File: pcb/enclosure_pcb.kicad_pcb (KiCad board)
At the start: 2 copper layers, 77.2 x 72.2 mm, 95 parts, among them J1 Conn_01x03_Pin, J3 USB_C_Receptacle_USB2.0_14P, J4 Conn_01x03_Pin, J5 Conn_01x03_Pin, J6 Conn_02x12_Odd_Even, J7 Conn_01x04_Pin, J8 Conn_ARM_JTAG_SWD_10, Q1 S8050, Q2 2SC3357-T1-A, Q3 MMBT918, SW1 SW_Push_WE, SW2 SW_Lever_RSPRO_5MS1, SW3 SW_Push_WE, U1 STM32F446RETx, U2 LD1117S33TR_SOT223, U3 LD1117S50TR_SOT223, U4 USBLC6-4SC6, U6 LM358_C5252902, Y1 Crystal_GND3, Y2 Crystal_4-pin

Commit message: V2_avant_revision
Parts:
- moved R23 158.8 mm to (161.5, 45.7), turned to -90 degrees
- moved J7 134.4 mm to (173.1, 66.0), turned to -90 degrees
- moved Y1 123.8 mm to (111.1, 52.5), turned to 90 degrees
- moved J5 116.2 mm to (125.1, 62.6), turned to 90 degrees
- moved R21 93.2 mm to (143.1, 75.5), turned to 90 degrees
- moved C27 89.3 mm to (197.9, 113.9), turned to 90 degrees
- moved F2 87.9 mm to (193.5, 103.4), turned to 180 degrees
- moved R29 81.6 mm to (146.7, 127.7), turned to 90 degrees
- moved D9 80.3 mm to (184.2, 108.1)
- moved C14 79.6 mm to (185.2, 102.4), turned to 180 degrees
- moved J1 78.6 mm to (145.6, 98.0), turned to -90 degrees
- moved U4 77.5 mm to (157.1, 123.5)
- moved R26 76.1 mm to (143.8, 127.7), turned to 90 degrees
- moved R28 75.0 mm to (140.5, 127.7), turned to 90 degrees
- moved U2 73.6 mm to (191.3, 111.0), turned to 90 degrees
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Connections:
- J6 pad 15: /SCH_MCU/PA2 -> /SCH_MCU/PA0
- J6 pad 19: /SCH_MCU/PA0 -> /SCH_MCU/PA2
- J6 pad 5: /SCH_MCU/PC6 -> /SCH_MCU/PC8
- J6 pad 9: /SCH_MCU/PC8 -> /SCH_MCU/PC6
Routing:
- net +5V: track 180.8 -> 352.2 mm, vias 7 -> 6
- net +3V3: track 254.6 -> 327.7 mm, vias 13 -> 4
- net /SCH_MCU/USB_DN: track 35.3 -> 93.6 mm, vias 0 -> 4
- net /SCH_MCU/USB_DP: track 35.3 -> 90.6 mm, vias 0 -> 2
- net /SCH_MCU/SWO: track 0.00 -> 44.5 mm, vias 0 -> 2
- net (no net): track 41.8 -> 0.00 mm, vias 2 -> 0
- net /SCH_FS1000/DATA IN: track 18.8 -> 60.3 mm
- net /SCH_MCU/PWM: track 26.9 -> 67.9 mm, vias 2 -> 0
- net /SCH_MCU/SWDIO: track 23.5 -> 56.8 mm
- net /SCH_FS1000/DATA OUT: track 27.7 -> 55.8 mm
- net Net-(D9-K): track 0.00 -> 27.4 mm
- net Net-(U1-BOOT0): track 30.6 -> 4.95 mm
- net /SCH_MCU/PA3: track 32.4 -> 57.8 mm, vias 2 -> 1
- net +E5V: track 100.1 -> 76.8 mm, vias 4 -> 2
- net /SCH_MCU/PUSH_BTN: track 39.4 -> 61.5 mm, vias 4 -> 2
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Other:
- board size 77.2 x 72.2 mm -> 108 x 107.9 mm

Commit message: V2_avant_revision_LOGO
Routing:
- net Net-(C18-Pad1): track 12.5 -> 46.0 mm, vias 0 -> 3
- net Net-(D1-A): track 0.00 -> 4.76 mm
- net Net-(C19-Pad2): track 18.1 -> 19.7 mm
- net +5V: track 352.2 -> 353.2 mm
- net /SCH_MCU/PB15: track 35.7 -> 36.7 mm
- net /SCH_MCU/PB14: track 37.7 -> 38.7 mm
- net GND: vias 112 -> 114
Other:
- board text added: "Author : Mario Flores Orihuela"
- board text added: "Rev: Cyprien Perrier"

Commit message: V2_avant_revision_LOGO
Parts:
- added G***: LOGO, images:LOGO_T, F.Cu at (192.4, 79.2)
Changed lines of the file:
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@@
 		)
 	)
+	(footprint "images:LOGO_T"
+		(layer "F.Cu")
+		(at 192.43 79.19)
+		(property "Reference" "G***"
+			(at 0 0 0)
+			(layer "F.SilkS")
+			(hide yes)
+			(effects
+				(font
+					(size 1.5 1.5)
+					(thickness 0.3)
+				)
+			)
+		)
+		(property "Value" "LOGO"
+			(at 0.75 0 0)
+			(layer "F.SilkS")
+			(hide yes)
+			(effects
+				(font
+					(size 1.5 1.5)
+					(thickness 0.3)
+				)
+			)
+		)
+		(property "Datasheet" ""
+			(at 0 0 0)
+			(layer "F.Fab")
+			(hide yes)
+			(effects
+				(font
+					(size 1.27 1.27)
+				)
+			)
+		)
+		(property "Description" ""
+			(at 0 0 0)
+			(layer "F.Fab")
+			(hide yes)
+			(effects
+				(font
+					(size 1.27 1.27)
+				)
+			)
+		)
+		(attr board_only exclude_from_pos_files exclude_from_bom)
+		(duplicate_pad_numbers_are_jumpers no)
+		(fp_poly
+			(pts
+				(xy -0.694939 -2.391834) (xy -0.721378 -2.011709) (xy -0.76683 -1.792088) (xy -0.825501 -1.725084)
+				(xy -0.941877 -1.720986) (xy -1.197332 -1.716317) (xy -1.561616 -1.711493) (xy -2.004476 -1.706928)
+				(xy -2.370667 -1.703917) (xy -3.810001 -1.693334) (xy -3.810001 0.677333) (xy -3.810001 3.047999)
+				(xy -4.572001 3.047999) (xy -5.334001 3.047999) (xy -5.334001 0.677333) (xy -5.334001 -1.693334)
+				(xy -6.900334 -1.693334) (xy -8.466667 -1.693334) (xy -8.466667 -2.370667) (xy -8.466667 -3.048001)
+				(xy -4.568439 -3.048001) (xy -0.670211 -3.048001)
+			)
+			(stroke
+				(width 0)
+				(type solid)
+			)
+			(fill yes)
+			(layer "F.SilkS")
+		)
+		(fp_poly
+			(pts
+				(xy -0.786473 -0.478819) (xy -0.429813 -0.359068) (xy -0.144081 -0.135991) (xy -0.019444 0.054578)
+				(xy 0.058089 0.24816) (xy 0.078587 0.367712) (xy 0.073748 0.377806) (xy -0.048275 0.415705) (xy -0.273934 0.432615)
+				(xy -0.53899 0.429732) (xy -0.779206 0.408253) (xy -0.930343 0.369374) (xy -0.945037 0.35883) (xy -1.085198 0.304234)
+				(xy -1.220845 0.352673) (xy -1.270001 0.456208) (xy -1.213292 0.558195) (xy -1.062439 0.742149)
+				(xy -0.846348 0.973712) (xy -0.770427 1.049994) (xy -0.525074 1.289113) (xy -0.37008 1.422703) (xy -0.276935 1.465837)
+				(xy -0.21713 1.433582) (xy -0.174781 1.364844) (xy -0.093646 1.261792) (xy 0.040013 1.207219) (xy 0.273513 1.186993)
+				(xy 0.426311 1.185333) (xy 0.693053 1.194996) (xy 0.875493 1.220102) (xy 0.929799 1.248833) (xy 0.890931 1.351471)
+				(xy 0.791523 1.55381) (xy 0.678745 1.764972) (xy 0.429225 2.217611) (xy 0.870779 2.629578) (xy 1.312333 3.041544)
+				(xy 0.683999 3.044772) (xy 0.278462 3.030542) (xy 0.020659 2.980931) (xy -0.08067 2.924617) (xy -0.191333 2.85282)
+				(xy -0.328485 2.852142) (xy -0.553003 2.920901) (xy -1.06616 3.029274) (xy -1.588033 3.008433) (xy -1.999616 2.885969)
+				(xy -2.349468 2.668926) (xy -2.55158 2.390633) (xy -2.623867 2.024944) (xy -2.624667 1.973773) (xy -2.615608 1.898135)
+				(xy -1.608667 1.898135) (xy -1.535706 2.044461) (xy -1.363233 2.154569) (xy -1.160863 2.200576)
+				(xy -0.998214 2.154599) (xy -0.989156 2.146265) (xy -1.007527 2.059537) (xy -1.123576 1.916666)
+				(xy -1.154375 1.887043) (xy -1.354563 1.754369) (xy -1.516297 1.739751) (xy -1.602846 1.842291)
+				(xy -1.608667 1.898135) (xy -2.615608 1.898135) (xy -2.58978 1.68247) (xy -2.461009 1.436532) (xy -2.365902 1.31984)
+				(xy -2.2101 1.128098) (xy -2.152272 0.983302) (xy -2.173529 0.809858) (xy -2.208069 0.688241) (xy -2.263431 0.444282)
+				(xy -2.240197 0.25981) (xy -2.146454 0.069846) (xy -1.894051 -0.220915) (xy -1.557389 -0.409464)
+				(xy -1.175264 -0.495526)
+			)
+			(stroke
+				(width 0)
+				(type solid)
+			)
+			(fill yes)
+			(layer "F.SilkS")
+		)
+		(fp_poly
+			(pts
+				(xy 8.043333 -2.413001) (xy 8.043333 -1.778001) (xy 5.138515 -1.778001) (xy 4.308888 -1.777258)
+				(xy 3.633459 -1.773605) (xy 3.097095 -1.764902) (xy 2.684661 -1.74901) (xy 2.381026 -1.723788) (xy 2.171054 -1.6871)
+				(xy 2.039612 -1.636804) (xy 1.971568 -1.570762) (xy 1.951786 -1.486834) (xy 1.965135 -1.382882)
+				(xy 1.977378 -1.331151) (xy 2.070017 -1.150176) (xy 2.180363 -1.066857) (xy 2.299282 -1.041241)
+				(xy 2.562667 -0.991004) (xy 2.948096 -0.920208) (xy 3.43315 -0.832916) (xy 3.995406 -0.733192) (xy 4.612446 -0.625097)
+				(xy 4.757347 -0.599896) (xy 5.546612 -0.458729) (xy 6.222334 -0.329427) (xy 6.772282 -0.214603)
+				(xy 7.184224 -0.116869) (xy 7.44593 -0.038839) (xy 7.509014 -0.012104) (xy 7.956251 0.296222) (xy 8.263643 0.671745)
+				(xy 8.433197 1.089181) (xy 8.466917 1.52325) (xy 8.36681 1.948668) (xy 8.134881 2.340153) (xy 7.773135 2.672422)
+				(xy 7.283578 2.920193) (xy 7.276196 2.922811) (xy 7.134579 2.960926) (xy 6.9378 2.990908) (xy 6.666948 3.013592)
+				(xy 6.303113 3.02981) (xy 5.827384 3.040394) (xy 5.220852 3.046179) (xy 4.464607 3.047997) (xy 4.434354 3.047999)
+				(xy 1.947333 3.047999) (xy 1.947333 2.416717) (xy 1.947333 1.785434) (xy 4.363509 1.76055) (xy 5.082198 1.751979)
+				(xy 5.649362 1.742029) (xy 6.082807 1.729617) (xy 6.400341 1.71366) (xy 6.61977 1.693074) (xy 6.758902 1.666776)
+				(xy 6.835544 1.633682) (xy 6.859879 1.608666) (xy 6.937603 1.375955) (xy 6.876962 1.181571) (xy 6.788128 1.108584)
+				(xy 6.667786 1.073515) (xy 6.402726 1.014622) (xy 6.015205 0.936242) (xy 5.52748 0.842716) (xy 4.961808 0.738383)
+				(xy 4.340445 0.627583) (xy 4.155587 0.595309) (xy 3.372144 0.457236) (xy 2.736601 0.339172) (xy 2.229547 0.235042)
+				(xy 1.83157 0.138771) (xy 1.523258 0.044283) (xy 1.285199 -0.054496) (xy 1.097982 -0.163642) (xy 0.942194 -0.289229)
+				(xy 0.798424 -0.437333) (xy 0.776373 -0.462232) (xy 0.560029 -0.754829) (xy 0.450164 -1.047178)
+				(xy 0.428089 -1.403521) (xy 0.442564 -1.60969) (xy 0.567667 -2.077273) (xy 0.842266 -2.470307) (xy 1.260031 -2.780516)
+				(xy 1.387091 -2.844618) (xy 1.502505 -2.896954) (xy 1.613371 -2.939356) (xy 1.738076 -2.972875)
+				(xy 1.895006 -2.998563) (xy 2.102549 -3.017469) (xy 2.379091 -3.030644) (xy 2.74302 -3.039138) (xy 3.212721 -3.044004)
+				(xy 3.806583 -3.046291) (xy 4.542992 -3.047049) (xy 4.931833 -3.047174) (xy 8.043333 -3.048001)
+			)
+			(stroke
+				(width 0)
+				(type solid)
+			)
+			(fill yes)
+			(layer "F.SilkS")
+		)
+		(embedded_fonts no)
+	)
 	(footprint "LED_SMD:LED_0603_1608Metric"
 		(layer "F.Cu")
@@
 	)
 	(gr_text "Rev: Cyprien Perrier\n"
-		(at 180.02 90.45 0)
+		(at 181.41 89.15 0)
 		(layer "F.SilkS")
 		(effects
@@
 	)
 	(gr_text "Author : Mario Flores Orihuela"
-		(at 180.1 88.89 0)
+		(at 181.49 87.59 0)
 		(layer "F.SilkS")
 		(effects
@@
 		)
 		(min_thickness 0.25)
-		(fill
+		(fill yes
 			(thermal_gap 0.5)
 			(thermal_bridge_width 0.5)
@@
 		)
 		(min_thickness 0.25)
-		(fill
+		(fill yes
 			(thermal_gap 0.5)
 			(thermal_bridge_width 0.5)

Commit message: fix(layout): footprints
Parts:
- removed J1: Conn_01x03_Pin, Connector_PinHeader_2.54mm:PinHeader_1x03_P2.54mm_Vertical
- added JP1: SolderJumper_2_Bridged, Jumper:SolderJumper-2_P1.3mm_Bridged_RoundedPad1.0x1.5mm, F.Cu at (115.2, 159.3)
- added SW4: SW_Push_WE, library:SW_Tactile_SPST_Angled_WE, F.Cu at (122.0, 157.7)
- AE1, AE2: footprint Connector_PinHeader_1.00mm:PinHeader_1x01_P1.00mm_Vertical -> library:AntennaHole
- J4: footprint Connector_JST:JST_XA_B03B-XASK-1-A_1x03_P2.50mm_Vertical -> Connector_JST:JST_XH_B3B-XH-A_1x03_P2.50mm_Vertical
- L5: footprint EasyEDA:IND-SMD_L10.2-W10.2-LS10.8 -> Inductor_SMD:L_0805_2012Metric
- L6: footprint EasyEDA:IND-SMD_L1.8-W1.2 -> Inductor_SMD:L_0603_1608Metric
- L7, L8: footprint EasyEDA:IND-SMD_L1.0-W0.5-2 -> Inductor_SMD:L_0603_1608Metric
- moved SW3 0.42 mm to (120.3, 136.8)
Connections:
- J8 pad 3: GND -> Net-(JP1-B)
- J8 pad 5: GND -> Net-(JP1-B)
- R7 pad 2: Net-(J1-Pin_2) -> GND
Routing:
- net Net-(J1-Pin_2): track 3.34 -> 0.00 mm
- net GND: track 2.49 -> 5.83 mm

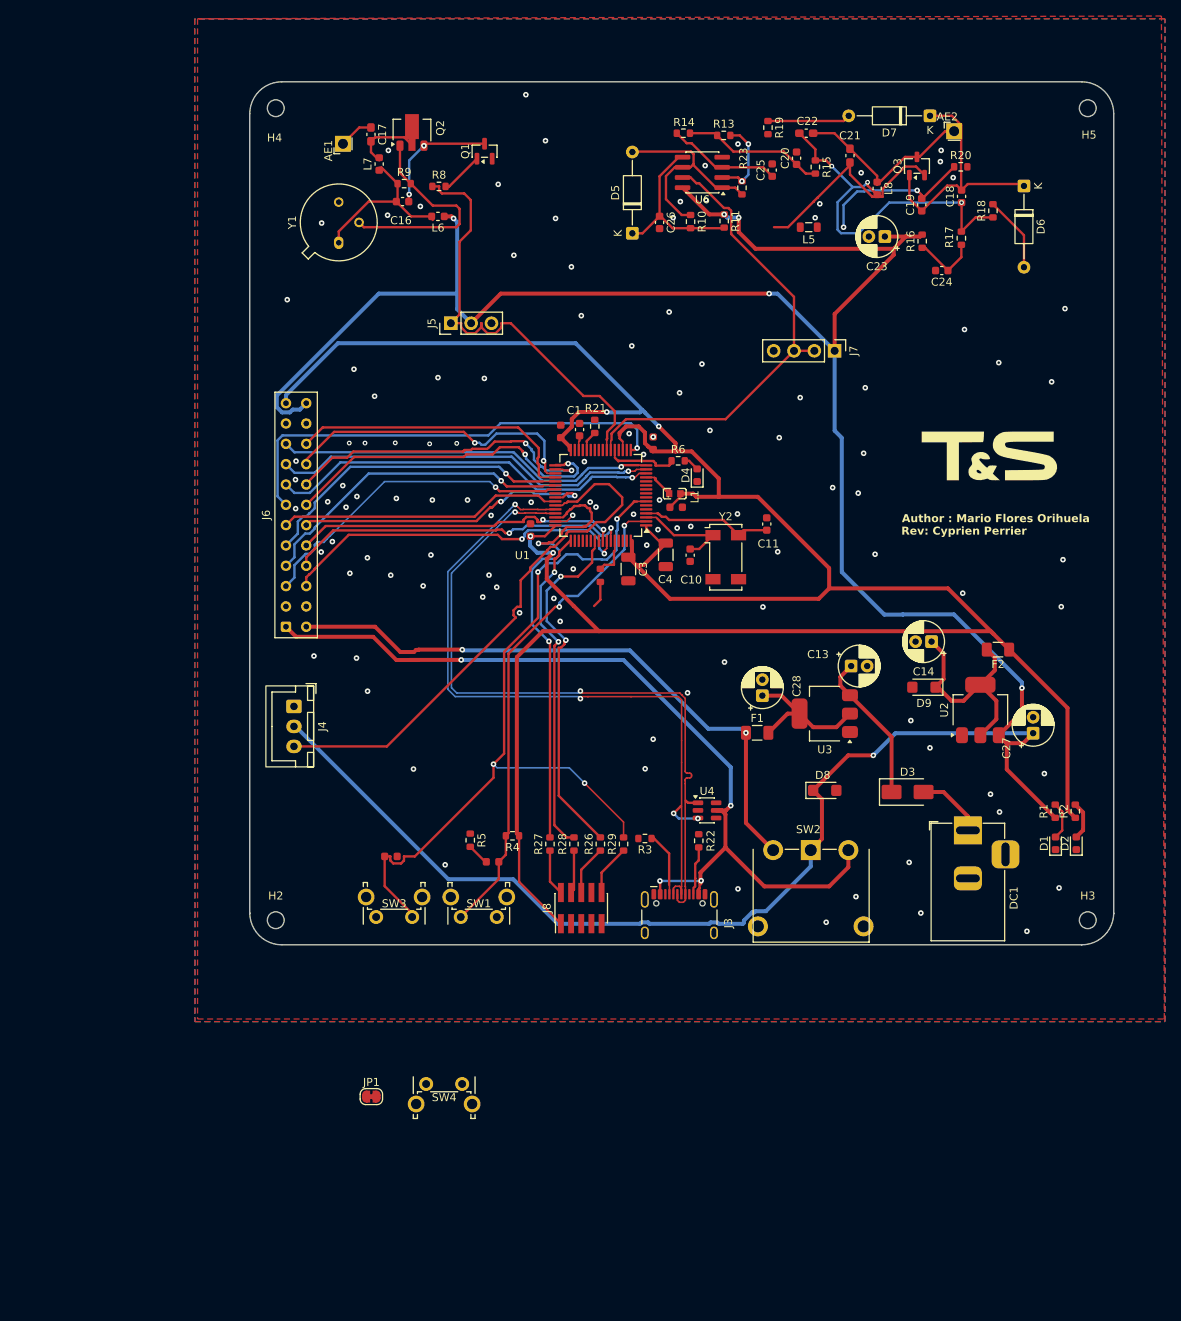
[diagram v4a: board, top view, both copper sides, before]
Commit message: feat(layout): component placement
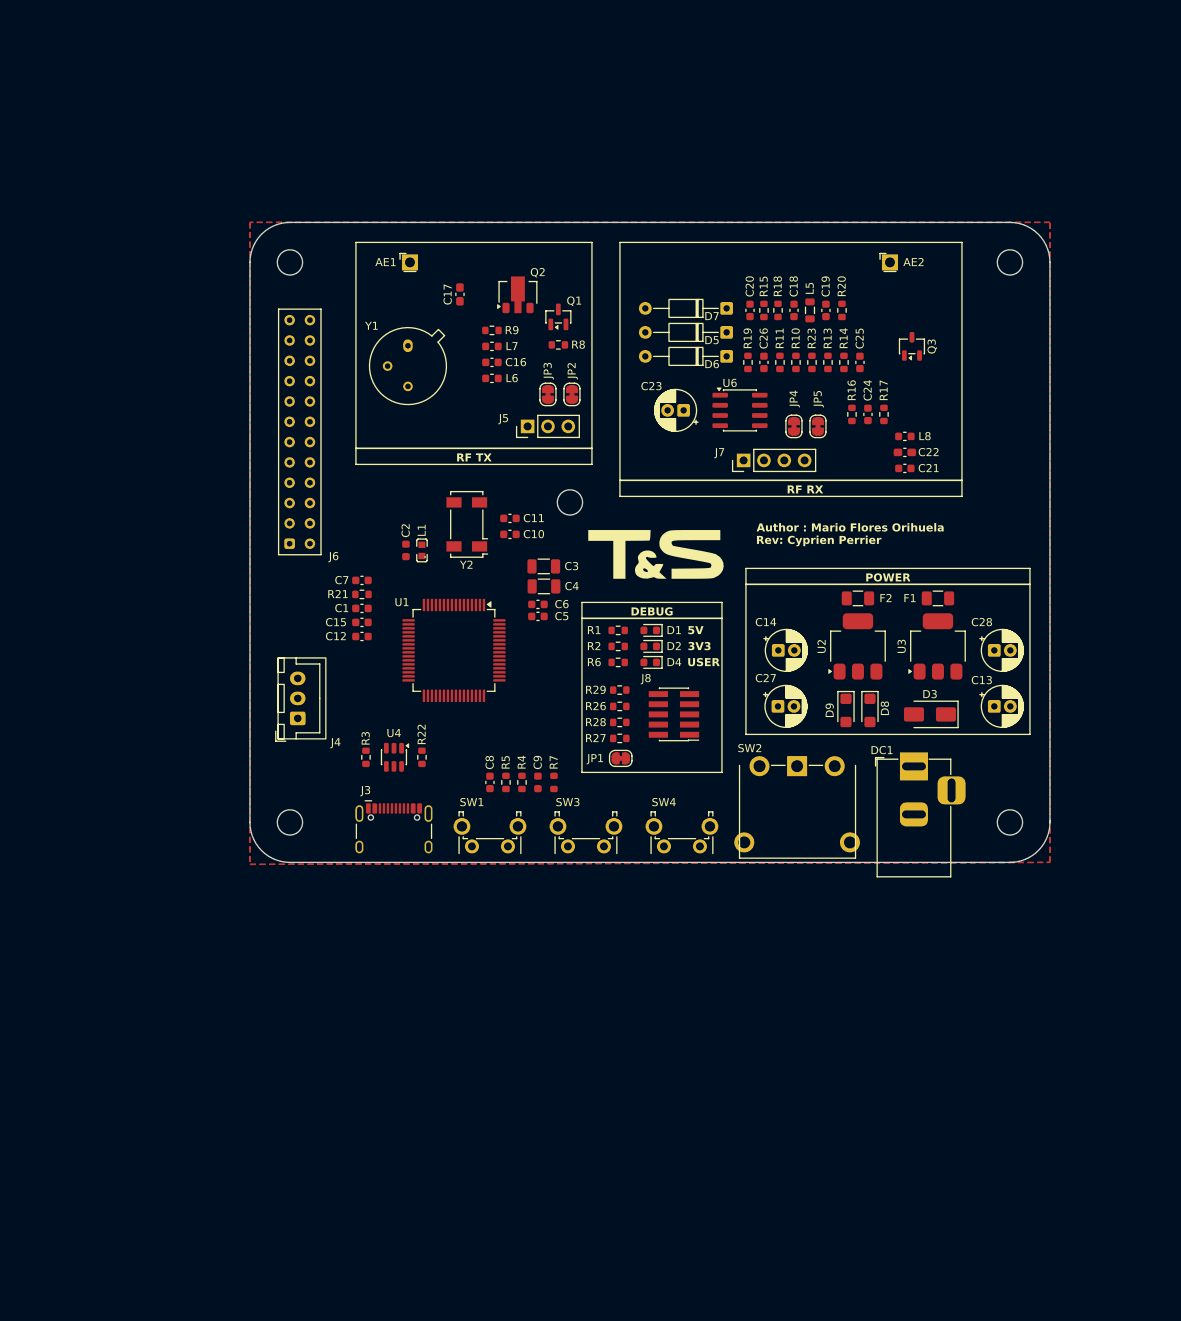
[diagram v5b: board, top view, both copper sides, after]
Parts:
- added ?: , , F.Cu at (140.0, 85.0)
- added C12: 1uF, Capacitor_SMD:C_0603_1608Metric, F.Cu at (114.0, 101.8)
- added C15: 1uF, Capacitor_SMD:C_0603_1608Metric, F.Cu at (114.0, 100.0)
- added JP2: SolderJumper_2_Bridged, Jumper:SolderJumper-2_P1.3mm_Bridged_RoundedPad1.0x1.5mm, F.Cu at (140.2, 71.5)
- added JP3: SolderJumper_2_Bridged, Jumper:SolderJumper-2_P1.3mm_Bridged_RoundedPad1.0x1.5mm, F.Cu at (137.2, 71.5)
- added JP4: SolderJumper_2_Bridged, Jumper:SolderJumper-2_P1.3mm_Bridged_RoundedPad1.0x1.5mm, F.Cu at (168.0, 75.5)
- added JP5: SolderJumper_2_Bridged, Jumper:SolderJumper-2_P1.3mm_Bridged_RoundedPad1.0x1.5mm, F.Cu at (171.0, 75.5)
- C21: footprint Capacitor_SMD:C_0603_1608Metric_Pad1.08x0.95mm_HandSolder -> Capacitor_SMD:C_0603_1608Metric
- C5, C6, C7, C8: footprint PCM_JLCPCB:C_0603 -> Capacitor_SMD:C_0603_1608Metric
- moved R2 60.7 mm to (146.0, 103.0), turned to 180 degrees
- moved R1 59.1 mm to (146.0, 101.0), turned to 180 degrees
- moved D2 58.7 mm to (150.0, 103.0), turned to 180 degrees
- moved D1 57.2 mm to (150.0, 101.0), turned to 180 degrees
- moved JP1 52.5 mm to (146.3, 117.0)
- moved SW4 45.3 mm to (156.2, 128.0), turned to 180 degrees
- moved G*** 43.5 mm to (150.8, 91.5)
- moved D6 42.8 mm to (159.6, 66.8), turned to 180 degrees
- moved C22 41.8 mm to (181.9, 78.8), turned to 0 degrees
- moved C7 40.2 mm to (114.0, 94.8), turned to 180 degrees
- moved C21 39.7 mm to (181.9, 80.8), turned to 180 degrees
- moved U4 39.7 mm to (118.0, 116.9), turned to -90 degrees
- moved J3 37.3 mm to (118.0, 127.0)
- moved R3 36.3 mm to (114.5, 116.9), turned to -90 degrees
- moved R22 36.1 mm to (121.5, 116.9)
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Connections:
- C23 pad 1: +5V -> /SCH_FS1000/5V_XY
- J5 pad 1: /SCH_FS1000/DATA OUT -> GND
- J5 pad 3: GND -> /SCH_FS1000/DATA_OUT
- J7 pad 1: +5V -> GND
- J7 pad 2: /SCH_FS1000/DATA IN -> /SCH_FS1000/DATA_IN
- J7 pad 3: /SCH_FS1000/DATA IN -> /SCH_FS1000/DATA_IN
- J7 pad 4: GND -> +5V
- L6 pad 1: +5V -> /SCH_FS1000/5V_FS
- R11 pad 1: +5V -> /SCH_FS1000/5V_XY
- R16 pad 2: +5V -> /SCH_FS1000/5V_XY
- R8 pad 1: /SCH_FS1000/DATA OUT -> /SCH_FS1000/DATA_OUT_FS
- SW2 pad 1: +E5V -> +U5V
- SW2 pad 3: +U5V -> +E5V
- SW4 pad 2: +3V3 -> Net-(U1-BOOT0)
- SW4 pad 3: Net-(U1-BOOT0) -> +3V3
- U1 pad 22: /SCH_FS1000/DATA IN -> /SCH_MCU/DATA OUT
- U1 pad 23: /SCH_FS1000/DATA OUT -> /SCH_MCU/DATA IN
- U6 pad 7: /SCH_FS1000/DATA IN -> /SCH_FS1000/DATA_IN_XY
- U6 pad 8: +5V -> /SCH_FS1000/5V_XY
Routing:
- net +5V: track 353.2 -> 0.00 mm, vias 6 -> 0
- net +3V3: track 327.7 -> 0.00 mm, vias 4 -> 0
- net +U5V: track 110.8 -> 0.00 mm, vias 4 -> 0
- net /SCH_MCU/NRST: track 97.8 -> 0.00 mm, vias 4 -> 0
- net /SCH_MCU/USB_DN: track 93.6 -> 0.00 mm, vias 4 -> 0
- net /SCH_MCU/USB_DP: track 90.6 -> 0.00 mm, vias 2 -> 0
- net +E5V: track 76.8 -> 0.00 mm, vias 2 -> 0
- net /SCH_MCU/PWM: track 67.9 -> 0.00 mm
- net /SCH_MCU/PUSH_BTN: track 61.5 -> 0.00 mm, vias 2 -> 0
- net /SCH_FS1000/DATA IN: track 60.3 -> 0.00 mm
- net /SCH_MCU/PA3: track 57.8 -> 0.00 mm, vias 1 -> 0
- net /SCH_MCU/SWDIO: track 56.8 -> 0.00 mm, vias 2 -> 0
- net /SCH_FS1000/DATA OUT: track 55.8 -> 0.00 mm
- net /SCH_MCU/PA0: track 50.0 -> 0.00 mm, vias 1 -> 0
- net /SCH_MCU/PA1: track 48.7 -> 0.00 mm, vias 1 -> 0
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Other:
- board size 108 x 107.9 mm -> 100 x 80 mm
- board text added: "3V3"
- board text added: "5V"
- board text added: "DEBUG"
- board text added: "POWER"
- board text added: "RF RX"
- board text added: "RF TX"
- board text added: "USER"

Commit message: feat(drc): updated drc
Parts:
- removed ?: , 
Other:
- outline, holes or cut-outs redrawn
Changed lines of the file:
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@@
 		(capping no)
 		(filling no)
+		(zone_defaults)
 		(grid_origin 100 50)
 		(pcbplotparams
@@
 		(sheetname "/SCH_MCU/")
 		(sheetfile "sch_mcu.kicad_sch")
-		(units
-			(unit
-				(name "A")
-				(pins "SH" "A1" "A12" "B1" "B12" "A4" "A9" "B4" "B9" "A5" "B5" "A7" "B7"
-					"A6" "B6"
-				)
-			)
-		)
 		(attr smd)
 		(duplicate_pad_numbers_are_jumpers no)
@@
 		)
 		(pad "" np_thru_hole circle
-			(at -2.89 -2.605)
+			(at -2.89 -2.55)
 			(size 0.65 0.65)
 			(drill 0.65)
@@
 		)
 		(pad "" np_thru_hole circle
-			(at 2.89 -2.605)
+			(at 2.89 -2.55)
 			(size 0.65 0.65)
 			(drill 0.65)
@@
 		(sheetname "/SCH_PWR/")
 		(sheetfile "sch_pwr.kicad_sch")
-		(units
-			(unit
-				(name "A")
-				(pins "2" "1" "3")
-			)
-		)
 		(attr through_hole)
 		(duplicate_pad_numbers_are_jumpers no)
@@
 		(fp_line
 			(start -2.5 11.5)
-			(end 11.05 11.5)
+			(end 12 11.5)
 			(stroke
 				(width 0.05)
@@
 		)
 		(fp_line
-			(start 12 9.53)
+			(start 12 11.5)
 			(end 12 -1.5)
 			(stroke
@@
 		)
 	)
-	(footprint ""
-		(layer "F.Cu")
-		(at 140 85)
-		(property "Reference" ""
-			(at 0 0 0)
-			(layer "F.SilkS")
-			(effects
-				(font
-					(size 1.27 1.27)
-				)
-			)
-		)
-		(property "Value" ""
-			(at 0 0 0)
-			(layer "F.Fab")
-			(effects
-				(font
-					(size 1.27 1.27)
-				)
-			)
-		)
-		(property "Datasheet" ""
-			(at 0 0 0)
-			(layer "F.Fab")
-			(hide yes)
-			(effects
-				(font
-					(size 1.27 1.27)
-				)
-			)
-		)
-		(property "Description" ""
-			(at 0 0 0)
-			(layer "F.Fab")
-			(hide yes)
-			(effects
-				(font
-					(size 1.27 1.27)
-				)
-			)
-		)
-		(duplicate_pad_numbers_are_jumpers no)
-		(pad "" np_thru_hole circle
-			(at 0 0)
-			(size 3.15 3.15)
-			(drill 3.15)
-			(layers "*.Cu" "*.Mask")
-		)
-		(embedded_fonts no)
-	)
 	(footprint "Resistor_SMD:R_0603_1608Metric"
 		(layer "F.Cu")
@@
 	)
 	(gr_arc
-		(start 199.996438 124.811313)
-		(mid 198.601627 128.468181)
+		(start 200 125)
+		(mid 198.535534 128.535534)
 		(end 195 130)
 		(stroke
@@
 		)
 		(min_thickness 0.25)
-		(fill
+		(fill yes
 			(thermal_gap 0.5)
 			(thermal_bridge_width 0.5)
@@
 		)
 		(min_thickness 0.25)
-		(fill
+		(fill yes
 			(thermal_gap 0.5)
 			(thermal_bridge_width 0.5)
